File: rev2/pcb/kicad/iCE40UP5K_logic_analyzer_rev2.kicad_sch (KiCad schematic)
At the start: 179 parts, among them IC1 ICE40UP5K-SG48I, IC2 MIC5504-3.3YM5-TR, IC3 MIC5504-1.2YM5-TR, IC4 FT2232HL-TRAY, IC5 W25Q40CLSNIG, IC6 SN74LVC14ADBRE4, IC7 SN74LVC14ADBRE4, IC8 SN74LVC14ADBRE4, J1 USB B Female Connector, J2 61300611121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

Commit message: rev2 schematic fully sorted with cleanup and different sections
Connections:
- net +3V3: now also C28.1, C29.1, FB1.1; no longer C28.2, C29.2, FB1.2
- net GND: now also C28.2, C29.2; no longer C28.1, C29.1
- net FTDI_USB_RX_LED: now reaches D8.1 (K), IC4.29 (ACBUS3)
- net FTDI_RESET#: now reaches IC4.14 (RESET#), R5.2, TP28.1
- net FTDI_USB_TX_LED: now reaches D9.1 (K), IC4.30 (ACBUS4)
- net FTDI_VPHY: now reaches C33.2, C35.1, IC4.4 (VPHY), TP23.1
- net FTDI_VPHY: now also FB1.2; no longer FB1.1
- net FTDI_PWRSAV: now reaches IC4.59 (BCBUS7), R3.2, R4.1, TP9.1
- net FTDI_REF: now reaches IC4.6 (REF), R2.1, TP24.1
- net FTDI_VPLL: now reaches C32.2, C34.1, FB2.2, IC4.9 (VPLL)
- net FTDI_VPLL: now also TP25.1
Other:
- note added: "4A low => 4Y high"
- note added: "5A low => 5Y high"
- note added: "FTDI (USB-UART bridge IC) VPHY and VPLL filter circuits"
- note added: "FTDI (USB-UART bridge IC) oscillator circuit"
- note added: "FTDI CHIP (UART-USB BRIDGE IC)"
- note added: "FTDI POWER PINS"
- note added: "FTDI debug LEDs (UART RX and TX)"
- note removed: "4Y high"
- note removed: "5Y high"
- note removed: "UART-USB BRIDGE IC"
- moved on the sheet: C1, C10, C11, C12, C13, C14, C15, C16, C17, C18, C19, C2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

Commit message: SCHEMATIC passed design rule check (DRC).
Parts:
- removed J4, J5: 61300821121, Connector_THT_Wurth:J_Wurth_WR-PHD_61300821121, symbol 8_pin_2x4_61300821121:61300821121
- removed J6: 61300311121, Connector_THT_Wurth:J_Wurth_WR-PHD_61300311121, symbol 8_pin_2x4_61300821121:61300311121
- removed TP16: SPI_VCCIO1, TestPoint:TestPoint_Pad_D1.0mm, symbol Connector:TestPoint
- removed TP17: VPP_2V5, TestPoint:TestPoint_Pad_D1.0mm, symbol Connector:TestPoint
- removed TP19: VCC_2, TestPoint:TestPoint_Pad_D1.0mm, symbol Connector:TestPoint
- removed TP20: VCCIO_0, TestPoint:TestPoint_Pad_D1.0mm, symbol Connector:TestPoint
- removed TP30: VPLL, TestPoint:TestPoint_Pad_D1.0mm, symbol Connector:TestPoint
- removed TP31: VCORE_2, TestPoint:TestPoint_Pad_D1.0mm, symbol Connector:TestPoint
- removed TP32: VCCIO_3, TestPoint:TestPoint_Pad_D1.0mm, symbol Connector:TestPoint
- removed TP34: VCCIO_4, TestPoint:TestPoint_Pad_D1.0mm, symbol Connector:TestPoint
- removed TP35: PWREN#, TestPoint:TestPoint_Pad_D1.0mm, symbol Connector:TestPoint
- added J4, J5: 61300821121, LIB_2x4_61300821121:J_Wurth_WR-PHD_61300821121, symbol 3pin_header_1x3_61300311121:61300821121
- added J6: 61300311121, LIB_1x3_61300311121:J_Wurth_WR-PHD_61300311121, symbol 3pin_header_1x3_61300311121:61300311121
- FB1, FB2: footprint BLM18SP221SN1B -> Ferrite_bead_BLM18AG601SN1D:BLM18SP221SN1B
- IC4: footprint QFP50P1200X1200X160-64N -> UART_USB_bridge_FT2232HL:QFP50P1200X1200X160-64N
- IC6, IC7, IC8: footprint SOP65P780X200-14N -> Schmitt_trigger_buffer_SN74LVC14ADBRE4:SOP65P780X200-14N
- J7: footprint Connector_THT_Wurth:J_Wurth_WR-PHD_61300621121 -> LIB_2x4_61300821121:J_Wurth_WR-PHD_61300621121
- Q1: footprint SOT95P240X110-3N -> NMOS_2N7002H6327XTSA2:SOT95P240X110-3N
- S1: footprint OS102011MA1QN1 -> Slide_switch_SPDT_ON/ON_OS102011MA1QN1:OS102011MA1QN1
- S2: footprint L101011MS02Q -> Slide_switch_SPST_ON/OFF_L101011MS02Q:L101011MS02Q
- TP11: value VCCIO_2 -> VCCIO
- TP12: value VREGIN -> FTDI_VREGIN
- TP15: value VCC1 -> VCC
- TP26: value VCORE_1 -> FTDI_VCORE
- TP29: value VPLL -> FTDI_VCCIO
- Y1: footprint 830208214809 -> 12MHz_CMOS_clock_830208214809:830208214809
- renumbered R68_unp to R68_unp1
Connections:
- net CDONE: now also J6.3
- net CRESET_B: now also J6.2
- net CTS#: now also J5.8
- net FPGA_DBG0: now also J4.2
- net FPGA_DBG1: now also J4.4
- net FPGA_DBG2: now also J4.6
- net FPGA_DBG3: now also J4.8
- net FPGA_UART_RX: now also J5.2
- net FPGA_UART_TX: now also J5.4
- net GND: now also IC7.7 (GND), J4.1, J4.3, J4.5, J4.7, J5.1, J5.3, J5.5, J5.7, J6.1
- net RTS#: now also J5.6
- no-connect marks 30 -> 32
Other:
- note added: "FPGA SPI_VCCIO_1"
- note added: "FPGA VCC1"
- note added: "FPGA VCCIO_0"
- note added: "FPGA VCCIO_2"
- note added: "FPGA VCC_2"
- note added: "FPGA VPP_2V5"
- note added: "FTDI VCCIO_1 decoupling"
- note added: "FTDI VCCIO_2 decoupling"
- note added: "FTDI VCCIO_3 decoupling"
- note added: "FTDI VCCIO_4 decoupling"
- note added: "FTDI VCORE_1 decoupling"
- note added: "FTDI VCORE_2 decoupling"
- note added: "FTDI VCORE_3 decoupling"
- note added: "FTDI VREGIN decoupling and bulk"
- note added: "FTDI VREGOUT filter cap"
- note removed: "filter cap"
- moved on the sheet: C1, C10, C11, C12, C13, C14, C15, C16, C17, C18, C19, C20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

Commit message: LAYOUT all components placed relatively well. Time for wiring
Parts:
- D8: value USB_RX -> FTDI_RX
- D9: value USB_TX -> FTDI_TX
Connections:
- net FTDI_USB_RX_LED renamed FTDI_RX_LED#
- net FTDI_USB_TX_LED renamed FTDI_TX_LED#
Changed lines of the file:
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@@
 		)
 	)
-	(label "FTDI_USB_TX_LED"
+	(label "FTDI_TX_LED#"
 		(at 111.76 184.15 0)
 		(effects
@@
 		)
 	)
-	(label "FTDI_USB_TX_LED"
+	(label "FTDI_TX_LED#"
 		(at 160.02 251.46 0)
 		(effects
@@
 		)
 	)
-	(label "FTDI_USB_RX_LED"
+	(label "FTDI_RX_LED#"
 		(at 111.76 173.99 0)
 		(effects
@@
 		)
 	)
-	(label "FTDI_USB_RX_LED"
+	(label "FTDI_RX_LED#"
 		(at 160.02 248.92 0)
 		(effects
@@
 			)
 		)
-		(property "Value" "USB_RX"
+		(property "Value" "FTDI_RX"
 			(at 135.128 170.942 0)
 			(effects
@@
 			)
 		)
-		(property "Value" "USB_TX"
+		(property "Value" "FTDI_TX"
 			(at 135.128 181.61 0)
 			(effects

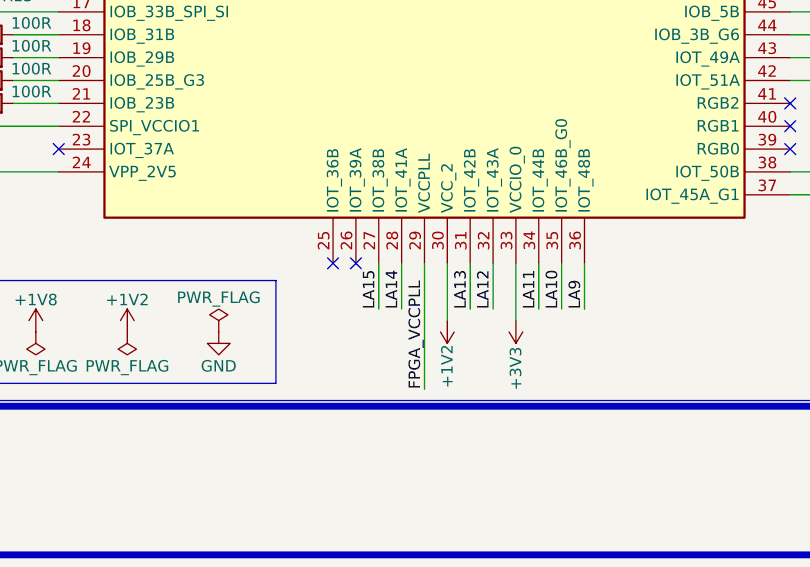
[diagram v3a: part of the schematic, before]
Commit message: LAYOUT. LA inputs sorted. Note that LA12-15 have new FPGA pins (updated in notes table and PCF).
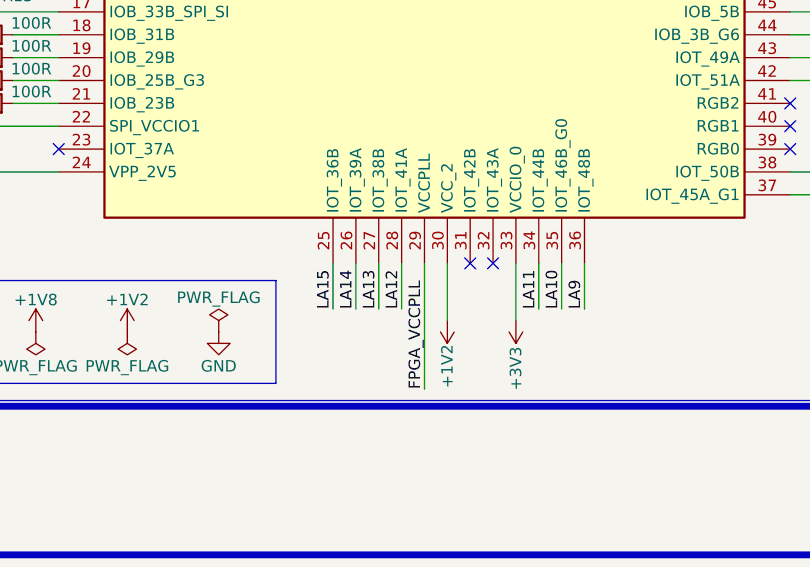
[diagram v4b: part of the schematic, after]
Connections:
- net LA12: now also IC1.28 (IOT_41A); no longer IC1.32 (IOT_43A)
- net LA13: now also IC1.27 (IOT_38B); no longer IC1.31 (IOT_42B)
- net LA14: now also IC1.26 (IOT_39A); no longer IC1.28 (IOT_41A)
- net LA15: now also IC1.25 (IOT_36B); no longer IC1.27 (IOT_38B)
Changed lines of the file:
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@@
 	)
 	(no_connect
+		(at 234.95 74.93)
+	)
+	(no_connect
 		(at 256.54 246.38)
 	)
@@
 	)
 	(no_connect
+		(at 232.41 74.93)
+	)
+	(no_connect
 		(at 210.82 264.16)
 	)
@@
 	)
 	(no_connect
-		(at 219.71 74.93)
-	)
-	(no_connect
-		(at 217.17 74.93)
-	)
-	(no_connect
 		(at 177.8 241.3)
 	)
@@
 	(wire
 		(pts
-			(xy 224.79 74.93) (xy 224.79 80.01)
-		)
-		(stroke
-			(width 0)
-			(type default)
-		)
-	)
-	(wire
-		(pts
 			(xy 210.82 209.55) (xy 212.09 209.55)
 		)
@@
 	(wire
 		(pts
+			(xy 222.25 74.93) (xy 222.25 80.01)
+		)
+		(stroke
+			(width 0)
+			(type default)
+		)
+	)
+	(wire
+		(pts
 			(xy 337.82 119.38) (xy 342.9 119.38)
 		)
@@
 	(wire
 		(pts
-			(xy 102.87 123.19) (xy 96.52 123.19)
+			(xy 219.71 74.93) (xy 219.71 80.01)
 		)
 		(stroke
@@
 	(wire
 		(pts
-			(xy 350.52 196.85) (xy 350.52 201.93)
+			(xy 102.87 123.19) (xy 96.52 123.19)
 		)
 		(stroke
@@
 	(wire
 		(pts
-			(xy 400.05 134.62) (xy 400.05 161.29)
+			(xy 350.52 196.85) (xy 350.52 201.93)
 		)
 		(stroke
@@
 	(wire
 		(pts
-			(xy 147.32 204.47) (xy 144.78 204.47)
+			(xy 400.05 134.62) (xy 400.05 161.29)
 		)
 		(stroke
@@
 	(wire
 		(pts
-			(xy 276.86 173.99) (xy 290.83 173.99)
+			(xy 147.32 204.47) (xy 144.78 204.47)
 		)
 		(stroke
@@
 	(wire
 		(pts
-			(xy 77.47 181.61) (xy 92.71 181.61)
+			(xy 276.86 173.99) (xy 290.83 173.99)
 		)
 		(stroke
@@
 	(wire
 		(pts
-			(xy 222.25 74.93) (xy 222.25 80.01)
+			(xy 77.47 181.61) (xy 92.71 181.61)
 		)
 		(stroke
@@
 	(wire
 		(pts
+			(xy 217.17 74.93) (xy 217.17 80.01)
+		)
+		(stroke
+			(width 0)
+			(type default)
+		)
+	)
+	(wire
+		(pts
 			(xy 242.57 22.86) (xy 242.57 29.21)
 		)
@@
 	(wire
 		(pts
+			(xy 224.79 74.93) (xy 224.79 80.01)
+		)
+		(stroke
+			(width 0)
+			(type default)
+		)
+	)
+	(wire
+		(pts
 			(xy 256.54 218.44) (xy 264.16 218.44)
 		)
@@
 	(wire
 		(pts
-			(xy 234.95 74.93) (xy 234.95 80.01)
-		)
-		(stroke
-			(width 0)
-			(type default)
-		)
-	)
-	(wire
-		(pts
 			(xy 19.05 62.23) (xy 19.05 64.77)
 		)
@@
 	(wire
 		(pts
-			(xy 232.41 74.93) (xy 232.41 80.01)
-		)
-		(stroke
-			(width 0)
-			(type default)
-		)
-	)
-	(wire
-		(pts
 			(xy 276.86 153.67) (xy 290.83 153.67)
 		)
@@
 		)
 	)
+	(label "LA15"
+		(at 217.17 80.01 90)
+		(effects
+			(font
+				(size 1.27 1.27)
+			)
+			(justify left bottom)
+		)
+	)
 	(label "SPI_CLK"
 		(at 88.9 132.08 180)
@@
 		)
 	)
+	(label "LA14"
+		(at 219.71 80.01 90)
+		(effects
+			(font
+				(size 1.27 1.27)
+			)
+			(justify left bottom)
+		)
+	)
 	(label "LA2"
 		(at 377.19 116.84 180)
@@
 		)
 	)
-	(label "LA13"
-		(at 232.41 80.01 90)
-		(effects
-			(font
-				(size 1.27 1.27)
-			)
-			(justify left bottom)
-		)
-	)
 	(label "LA7_raw"
 		(at 406.4 233.68 180)
@@
 		)
 	)
+	(label "LA12"
+		(at 224.79 80.01 90)
+		(effects
+			(font
+				(size 1.27 1.27)
+			)
+			(justify left bottom)
+		)
+	)
+	(label "LA13"
+		(at 222.25 80.01 90)
+		(effects
+			(font
+				(size 1.27 1.27)
+			)
+			(justify left bottom)
+		)
+	)
 	(label "FPGA_DBG0"
 		(at 48.26 181.61 180)
@@
 		)
 	)
-	(label "LA15"
-		(at 222.25 80.01 90)
-		(effects
-			(font
-				(size 1.27 1.27)
-			)
-			(justify left bottom)
-		)
-	)
 	(label "FPGA_VCCPLL"
 		(at 227.33 88.9 90)
@@
 	)
 	(label "LA14"
-		(at 224.79 80.01 90)
-		(effects
-			(font
-				(size 1.27 1.27)
-			)
-			(justify left bottom)
-		)
-	)
-	(label "LA14"
 		(at 396.24 191.77 180)
 		(effects
@@
 		(effects
 			(font
-				(size 1.27 1.27)
-			)
-			(justify left bottom)
-		)
-	)
-	(label "LA12"
-		(at 234.95 80.01 90)
-		(effects
-			(font
